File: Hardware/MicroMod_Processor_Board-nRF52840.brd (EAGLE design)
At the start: 22 x 22 mm, 30 parts, among them J1 MICROMOD-2222, U1 W25QXX128MBIT-6X5, U2 MDBT50Q, Y1 32.768kHz

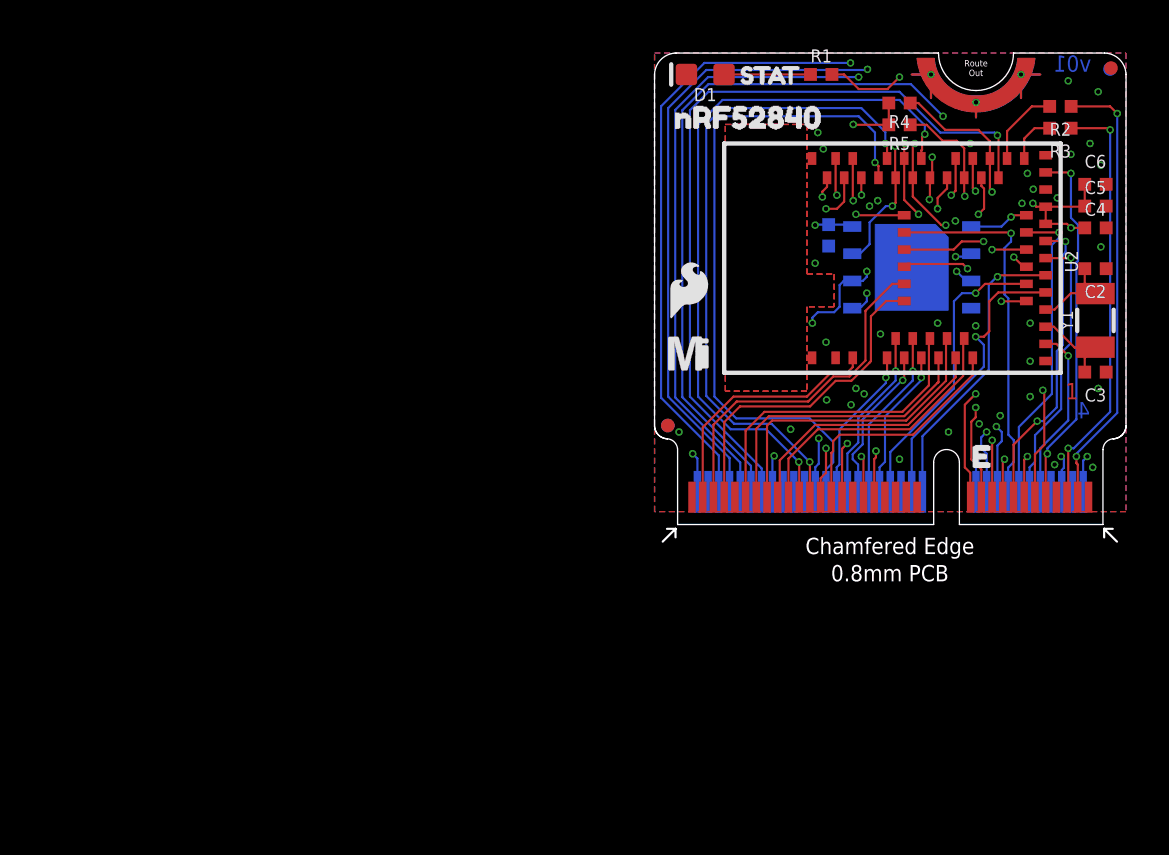
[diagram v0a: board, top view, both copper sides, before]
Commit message: Schematic updated post-proto testing
Changes made: https://docs.google.com/document/d/1057ZJf50zAkChxiBm4WqtqCuvZdJMlmnGmuK_T1RHvQ/edit
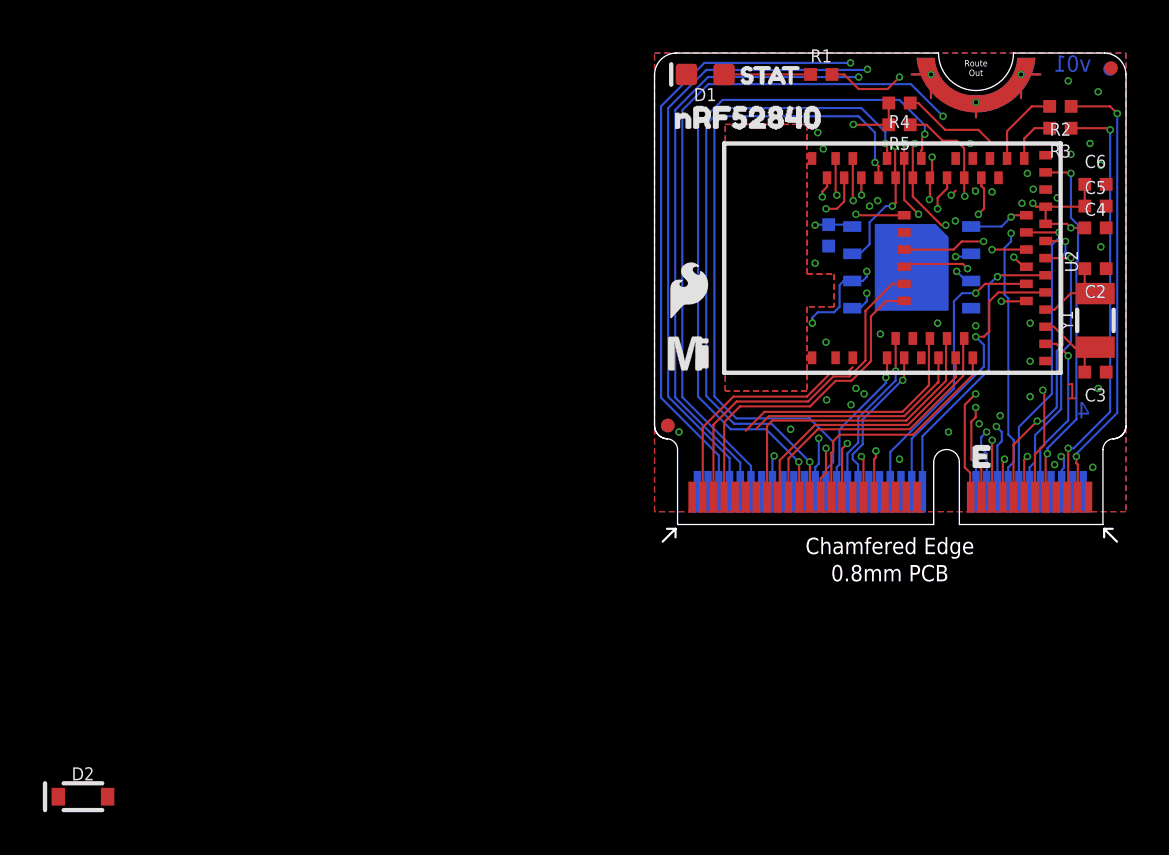
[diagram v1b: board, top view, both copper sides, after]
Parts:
- added D2: 1A/23V/620mV, SparkFun-DiscreteSemi:SOD-323
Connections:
- net SPI_MISO1 renamed SPI_CIPO
- net SPI_MOSI1 renamed SPI_COPI
- removed net ADC_D+: J1.63, U2.10
- removed net ADC_D-: J1.65, U2.9
- removed net GPIO0: J1.40, U2.8
- removed net GPIO1: J1.42, U2.7
- removed net SPI_!CS!1: J1.55, U2.44
- removed net SPI_MISO: J1.64, U1.5, U2.43
- removed net SPI_MOSI: J1.62, U2.36
- new net 3.3V_EN: J1.4, U2.8
- new net GPIO0-A: J1.40, U2.9
- new net GPIO1-A: J1.42, U2.10
- new net GPIO8: J1.67, U2.7
- new net N$5: D2.A, J1.2, J1.74
- new net SPI_!CS1!: J1.70, U1.7, U2.47
- new net SPI_CIPO1: J1.64, U1.2, U2.43
- new net SPI_COPI1: J1.62, U1.5, U2.36
- net !BOOT!: now also U2.23; no longer U2.37
- net 3.3V: now also D2.C, J1.72; no longer J1.2, J1.74
- net GPIO5: now also U2.41; no longer U2.3
- net I2C_!INT!: now also U2.39; no longer U2.60
- net LED_BUILTIN: now also U2.37; no longer U2.23
- net RX1: now also U2.3; no longer U2.41
- net SDIO_DATA1: no longer U1.2
- net SPI_!CS!: now also J1.55, U2.44; no longer J1.70, U1.7, U2.47
- net SPI_SCK: now also J1.57, U2.13; no longer J1.60, U1.6, U2.42
- net SPI_SCK1: now also J1.60, U1.6, U2.42; no longer J1.57, U2.13
- net TX1: now also U2.60; no longer U2.39
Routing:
- net SPI_MISO: track 44.8 -> 0.00 mm, vias 5 -> 0
- net SPI_CIPO1: track 0.00 -> 44.8 mm, vias 0 -> 5
- net SPI_!CS1!: track 0.00 -> 39.8 mm, vias 0 -> 3
- net SPI_MOSI: track 36.7 -> 0.00 mm, vias 1 -> 0
- net SPI_!CS!1: track 33.5 -> 0.00 mm, vias 2 -> 0
- net ADC_D-: track 14.7 -> 0.00 mm
- net ADC_D+: track 13.7 -> 0.00 mm
- net GPIO0-A: track 0.00 -> 11.6 mm
- net GPIO1-A: track 0.00 -> 10.5 mm
- net SPI_SCK1: track 13.3 -> 21.9 mm, vias 0 -> 5
- net SPI_SCK: track 21.9 -> 13.3 mm, vias 5 -> 0
- net GPIO1: track 8.00 -> 0.00 mm, vias 1 -> 0
- net GPIO0: track 7.06 -> 0.00 mm, vias 1 -> 0
- net SPI_!CS!: track 39.8 -> 33.5 mm, vias 3 -> 2
- net I2C_!INT!: track 17.5 -> 12.5 mm
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
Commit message: Routing for v10
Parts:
- moved D2 34.5 mm to (1.27, 7.62), turned to 270 degrees
- moved U$1 5.08 mm to (1.55, 13.1)
- moved LOGO2 5.08 mm to (1.60, 16.0)
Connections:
- net GPIO0-A: now also U2.10; no longer U2.9
- net GPIO1-A: now also U2.9; no longer U2.10
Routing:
- net N$5: track 0.00 -> 29.0 mm, vias 0 -> 3
- net SPI_COPI1: track 0.00 -> 22.7 mm, vias 0 -> 5
- net 3.3V_EN: track 0.00 -> 14.8 mm, vias 0 -> 3
- net GPIO8: track 0.00 -> 14.2 mm
- net GPIO5: track 11.4 -> 25.6 mm, vias 0 -> 3
- net SDIO_DATA1: track 40.0 -> 32.1 mm, vias 5 -> 2
- net LED_BUILTIN: track 15.5 -> 9.93 mm
- net SPI_CIPO1: track 44.8 -> 39.4 mm, vias 5 -> 4
- net I2C_!INT!: track 12.5 -> 17.5 mm
- net GPIO0-A: track 11.6 -> 7.39 mm, vias 0 -> 1
- net !BOOT!: track 21.3 -> 24.5 mm
- net RX1: track 16.3 -> 13.3 mm
- net 3.3V: track 10.7 -> 13.5 mm, vias 4 -> 6
- net GPIO1-A: track 10.5 -> 8.34 mm, vias 0 -> 1
- net TX1: track 15.4 -> 17.2 mm
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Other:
- board text added: "v10"
- board text removed: "v01"

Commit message: Update MicroMod_Processor_Board-nRF52840.brd
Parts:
- removed U$4: (no value), SparkFun-Buzzard:STAT_TO_32
- added U$6: (no value), output:NRF528400
- U$2: device buzzard_labels (79):NRF528400 -> output:STAT0
- U$3: device buzzard_labels (80):NRF528400 -> output:NRF528400
- moved U$2 18.9 mm to (5.40, 21.0), flipped to the top
- moved U$3 17.2 mm to (10.8, 5.59), flipped to the bottom
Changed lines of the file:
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@@
 <?xml version="1.0" encoding="utf-8"?>
 <!DOCTYPE eagle SYSTEM "eagle.dtd">
-<eagle version="9.4.2">
+<eagle version="9.6.0">
 <drawing>
 <settings>
@@
 <setting verticaltext="up"/>
 </settings>
-<grid distance="0.05" unitdist="inch" unit="inch" style="lines" multiple="1" display="yes" altdistance="0.005" altunitdist="inch" altunit="inch"/>
+<grid distance="0.05" unitdist="inch" unit="inch" style="lines" multiple="1" display="yes" altdistance="0.0025" altunitdist="inch" altunit="inch"/>
 <layers>
 <layer number="1" name="Top" color="4" fill="1" visible="yes" active="yes"/>
@@
 <element name="LOGO1" library="SparkFun-Aesthetics" package="SFE_LOGO_NAME_FLAME_.1" value="SFE_LOGO_NAME_FLAME.1_INCH" x="11" y="16.79" smashed="yes" rot="MR0"/>
 <element name="LOGO2" library="SparkFun-Aesthetics" package="SFE_LOGO_FLAME_.1" value="SFE_LOGO_FLAME.1_INCH" x="1.599" y="16.032" smashed="yes"/>
-<element name="U$4" library="SparkFun-Buzzard" package="STAT_TO_32" value="" x="3.247" y="20.962" smashed="yes"/>
 <element name="U$1" library="SparkFun-MicroMod" package="MICROMOD_MI_LOGO_.35" value="" x="1.549" y="13.079" smashed="yes"/>
 <element name="U$5" library="SparkFun-MicroMod" package="MICROMOD_LOGO_.35" value="" x="11" y="7.3" smashed="yes" rot="MR0"/>
@@
 <attribute name="VALUE" x="11.43" y="19.214" size="0.6096" layer="27" font="vector" ratio="20" rot="R180" align="top-center"/>
 </element>
-<element name="U$2" library="buzzard_labels (79)" package="NRF528400" value="" x="16.36" y="5.58" smashed="yes" rot="MR0"/>
-<element name="U$3" library="buzzard_labels (80)" package="NRF528400" value="" x="0" y="19" smashed="yes"/>
 <element name="D2" library="SparkFun-DiscreteSemi" package="SOD-323" value="1A/23V/620mV" x="1.27" y="7.62" smashed="yes" rot="R270">
 <attribute name="NAME" x="2.032" y="7.62" size="0.6096" layer="25" font="vector" ratio="20" rot="R270" align="bottom-center"/>
@@
 <attribute name="VALUE" x="0.508" y="7.62" size="0.6096" layer="27" font="vector" ratio="20" rot="R270" align="top-center"/>
 </element>
+<element name="U$6" library="output" package="NRF528400" value="" x="5.334" y="18.923" smashed="yes"/>
+<element name="U$3" library="output" package="NRF528400" value="" x="10.795" y="5.588" smashed="yes" rot="MR0"/>
+<element name="U$2" library="output" package="STAT0" value="" x="5.3975" y="20.955" smashed="yes"/>
 </elements>
 <signals>

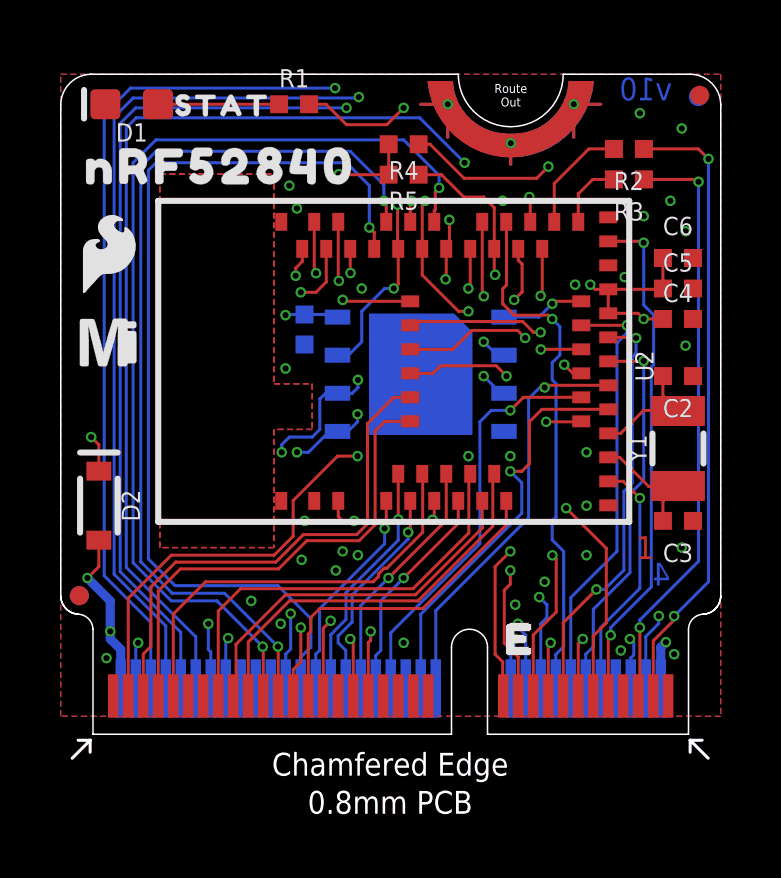
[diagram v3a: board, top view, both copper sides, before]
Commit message: Design review and checklist changes
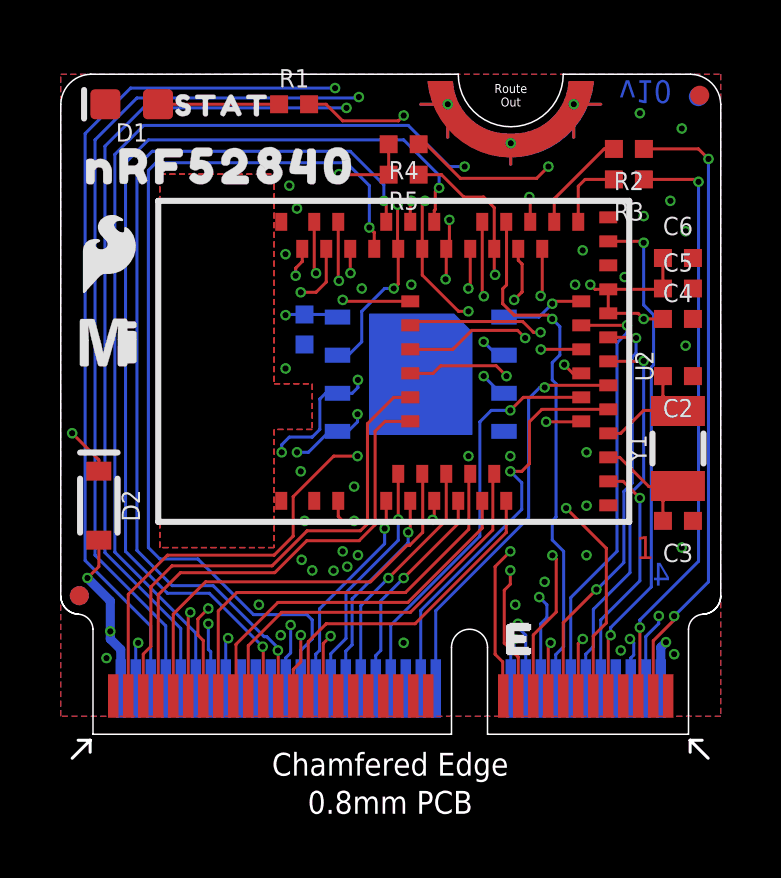
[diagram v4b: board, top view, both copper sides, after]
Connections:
- net GPIO0-A renamed GPIO0/ADC2
- net GPIO1-A renamed GPIO1/ADC3
- net SPI_!CS1! renamed SPI_!CS1!/SDIO_DATA3
- net SPI_CIPO1 renamed SPI_CIPO1/SDIO_DATA0
- net SPI_COPI1 renamed SPI_COPI1/SDIO_CMD
- net SPI_SCK1 renamed SPI_SCK1/SDIO_CLK
- removed net NFC1: J1.43, U2.52
- removed net NFC2: J1.41, U2.54
- new net GPIO10/NFC2: J1.63, U2.54
- new net GPIO9/NFC1: J1.65, U2.52
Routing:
- net GPIO10/NFC2: track 0.00 -> 19.4 mm, vias 0 -> 3
- net GPIO9/NFC1: track 0.00 -> 19.2 mm, vias 0 -> 3
- net NFC1: track 16.3 -> 0.00 mm, vias 2 -> 0
- net NFC2: track 16.2 -> 0.00 mm, vias 2 -> 0
- net SPI_COPI1/SDIO_CMD: track 22.7 -> 23.2 mm
- net SPI_!CS1!/SDIO_DATA3: track 38.8 -> 39.4 mm
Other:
- board text added: "0.8mm PCB 45 degree chamfered edge Four layer design ENIG Finish"
- board text removed: "0.8mm PCB 45 degree chamfered edge Four layer design"

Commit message: Updated variant files for new version of arduino core
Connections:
- net GPIO0/ADC2 renamed GPIO0
- net GPIO1/ADC3 renamed GPIO1
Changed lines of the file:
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@@
 <wire x1="8.001" y1="5.78615625" x2="8.001" y2="3.302" width="0.1016" layer="15"/>
 </signal>
-<signal name="GPIO0/ADC2">
+<signal name="GPIO0">
 <contactref element="J1" pad="40"/>
 <contactref element="U2" pad="10"/>
@@
 <wire x1="10.668" y1="2.794" x2="10.5" y2="2.626" width="0.1016" layer="16"/>
 </signal>
-<signal name="GPIO1/ADC3">
+<signal name="GPIO1">
 <contactref element="J1" pad="42"/>
 <contactref element="U2" pad="9"/>
